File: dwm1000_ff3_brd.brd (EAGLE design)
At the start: 61.4 x 28.4 mm, 19 parts, among them J3 AVR_SPI_PRG_6PTH

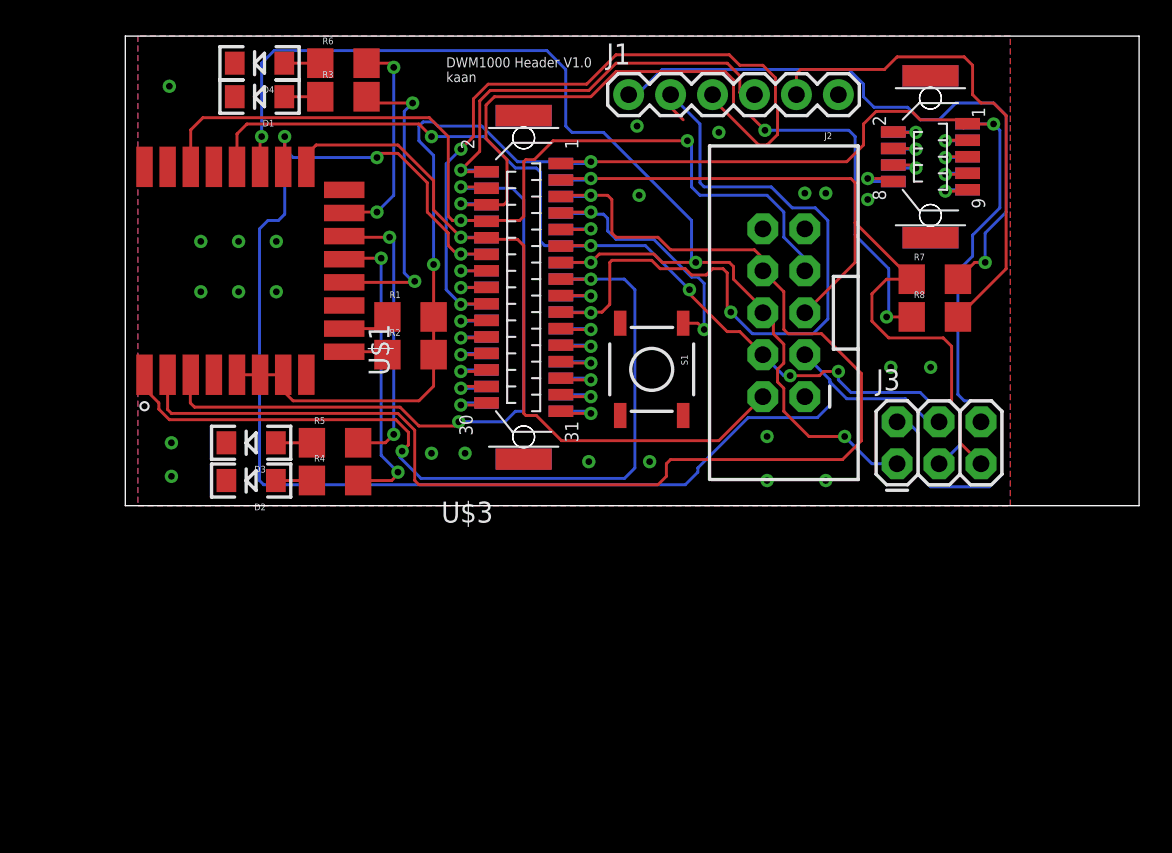
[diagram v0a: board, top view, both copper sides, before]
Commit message: added firefly DWM1000 module
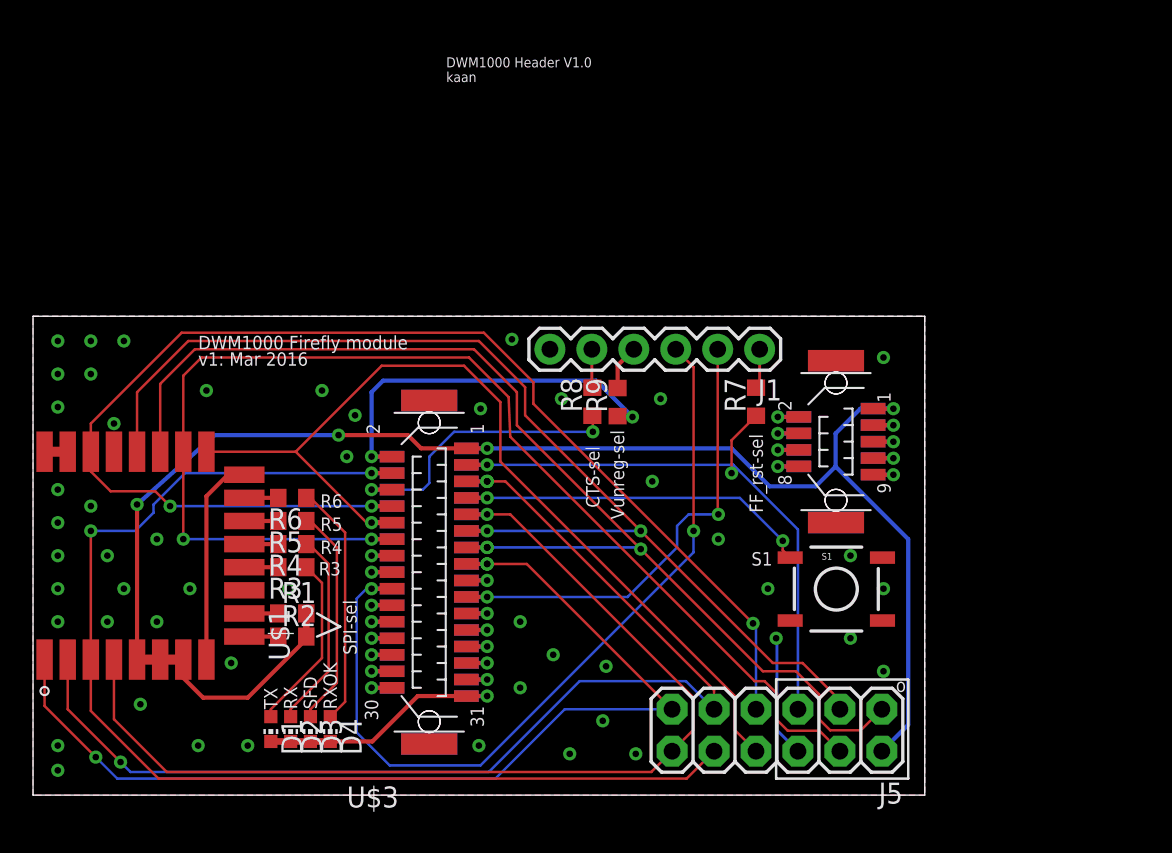
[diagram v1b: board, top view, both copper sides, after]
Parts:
- removed J2: (no value), SparkFun-Connectors:2X5-SHROUDED
- removed J3: AVR_SPI_PRG_6PTH, SparkFun-Connectors:2X3
- added J5: 2X6 FEMALE, SparkFun-Connectors:2X6
- added R9: 0, rcl:R0603
- D1, D2, D3, D4: device SparkFun-LED:LED-1206 -> led:CHIP-LED0603
- R1, R2, R3, R4, R5, R6, R7, R8: device SparkFun-Passives:1206 -> rcl:R0603
- moved D4 40.5 mm to (18.0, 4.00)
- moved D1 38.3 mm to (14.4, 4.00)
- moved R3 28.7 mm to (15.7, 13.8), turned to 180 degrees
- moved R6 26.5 mm to (15.7, 18.0), turned to 180 degrees
- moved R8 21.4 mm to (33.9, 23.8), turned to 90 degrees
- moved R1 19.3 mm to (15.7, 11.0)
- moved R2 18.5 mm to (15.7, 9.60)
- moved U$1 18.3 mm to (13.0, 14.5)
- moved U$2 18.2 mm to (40.0, 14.5)
- moved U$3 18.2 mm to (40.0, 14.5)
- moved D3 17.7 mm to (16.8, 4.00)
- moved S1 17.4 mm to (48.6, 12.5), turned to 0 degrees
- moved J1 17.3 mm to (44.0, 27.0), turned to 180 degrees
- moved D2 15.2 mm to (15.6, 4.00)
- moved R7 13.1 mm to (43.8, 23.8), turned to 90 degrees
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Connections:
- net PD1 renamed SW1
- net SCL renamed CTS
- removed net N$11: U$1.4
- removed net PB5: U$1.1, U$2.15, U$3.15
- removed net PG0: U$1.3, U$2.4, U$3.4
- removed net PG1: J2.8, U$1.2, U$2.5, U$3.5
- removed net RST: J2.5, J3.5, R7.1, U$2.3, U$3.3
- removed net RX1_MCU: J2.7, U$1.22, U$2.8, U$3.8
- removed net SYNC: J2.10
- removed net TX1_MCU: U$2.9, U$3.9
- new net DW_EXTON: J5.11, U$1.1, U$2.15, U$3.15
- new net DW_IRQ: J5.7, U$1.22, U$2.8, U$3.8
- new net DW_RSTN: J5.10, U$1.3, U$2.4, U$3.4
- new net DW_SYNC: J5.12, U$1.4, U$2.9, U$3.9
- new net DW_WAKE: J5.9, U$1.2, U$2.5, U$3.5
- new net FF_RSTN: J5.5, R7.1, U$2.3, U$3.3
- new net N$6: J1.4, R9.2
- net GND: now also J5.6; no longer J2.1, J2.9, J3.6
- net MISO: now also J5.1; no longer J2.6, J3.1
- net MOSI: now also J5.4; no longer J2.3, J3.4
- net SCK: now also J5.3; no longer J2.4, J3.3
- net SSN: now also J5.8; no longer J2.2
- net VDD: now also J5.2; no longer J3.2
- net V_UNREG: now also R9.1; no longer J1.4
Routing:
- net PG1: track 80.9 -> 0.00 mm, vias 1 -> 0
- net DW_IRQ: track 0.00 -> 79.0 mm, vias 0 -> 3
- net DW_RSTN: track 0.00 -> 72.3 mm, vias 0 -> 2
- net DW_WAKE: track 0.00 -> 69.4 mm, vias 0 -> 3
- net DW_SYNC: track 0.00 -> 62.6 mm, vias 0 -> 1
- net DW_EXTON: track 0.00 -> 61.7 mm, vias 0 -> 3
- net RX1_MCU: track 58.3 -> 0.00 mm, vias 2 -> 0
- net PB5: track 54.1 -> 0.00 mm, vias 2 -> 0
- net RST: track 51.5 -> 0.00 mm, vias 1 -> 0
- net PG0: track 41.4 -> 0.00 mm, vias 2 -> 0
- net FF_RSTN: track 0.00 -> 38.5 mm, vias 0 -> 2
- net N$18: track 37.4 -> 2.42 mm, vias 1 -> 0
- net GND: track 7.00 -> 39.6 mm, vias 26 -> 52
- net CTS: track 50.0 -> 18.0 mm, vias 3 -> 2
- net N$19: track 30.3 -> 2.34 mm
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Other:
- board size 61.4 x 28.4 mm -> 54 x 29 mm
- board text added: "CTS-sel"
- board text added: "DWM1000 Firefly module"
- board text added: "FF_rst-sel"
- board text added: "R3"
- board text added: "R4"
- board text added: "R5"
- board text added: "R6"
- board text added: "RX"
- board text added: "RXOK"
- board text added: "S1"
- board text added: "SFD"
- board text added: "SPI-sel"
- board text added: "TX"
- board text added: "Vunreg-sel"
- board text added: "kaan, and 2016"
- board text added: "o"
- board text added: "v1: Mar 2016"

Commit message: width change to 7mil, minor fix to gnd via
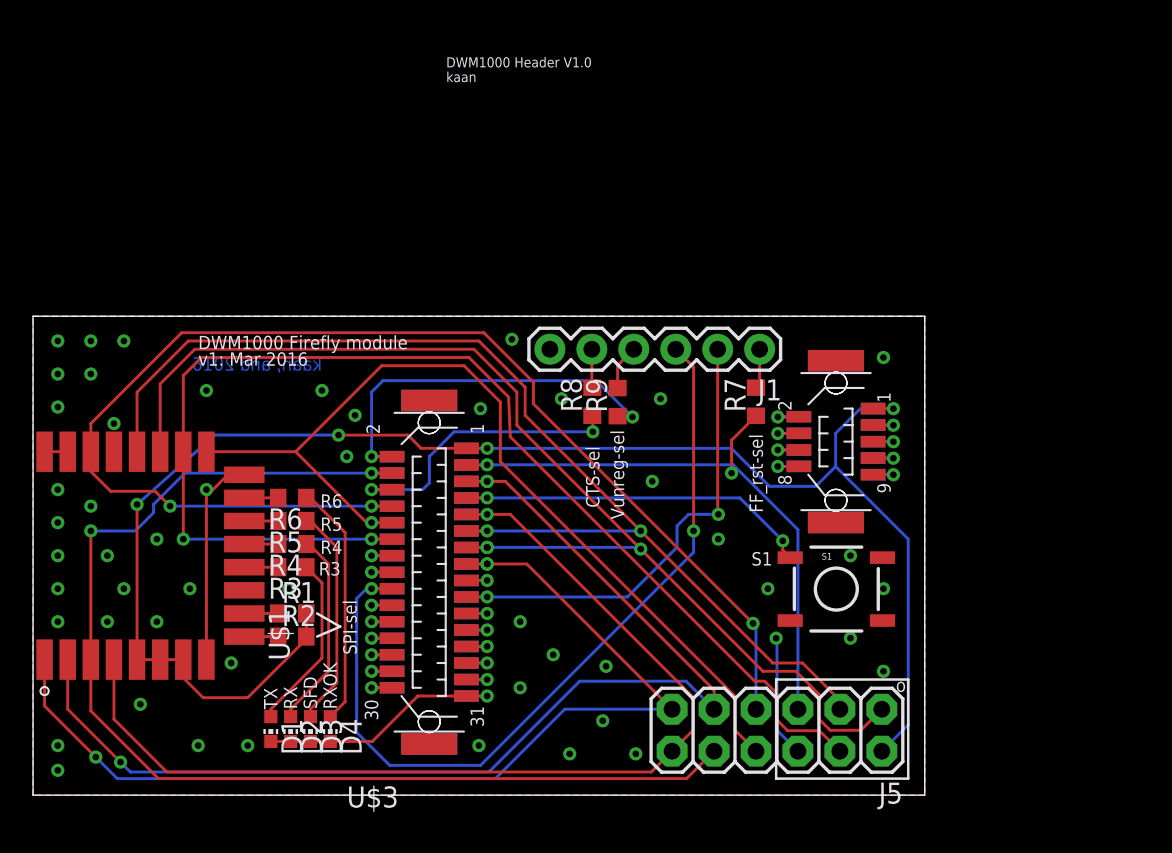
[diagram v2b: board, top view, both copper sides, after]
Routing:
- net GND: vias 52 -> 54
